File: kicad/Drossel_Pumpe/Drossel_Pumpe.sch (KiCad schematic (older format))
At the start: 6 parts, among them J1 Conn_02x01, M1 Pumpe

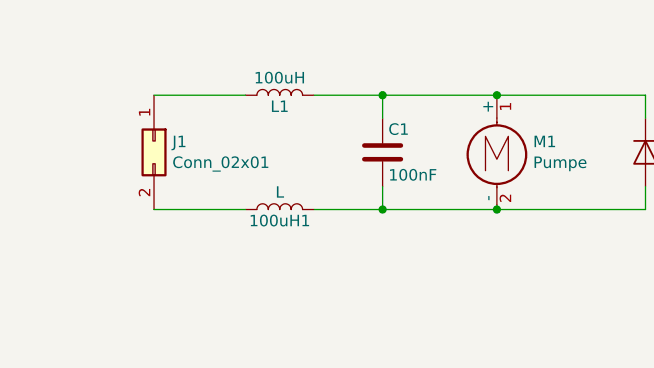
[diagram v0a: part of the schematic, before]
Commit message: umbenannt:      2019_Abschlussprojekt_Zuordnugstabelle.ods -> Doku/2019_Abschlussprojekt_Zuordnugstabelle.ods 	neue Datei:     Doku/Anmerungen_fuer_Doku.odt 	umbenannt:      Stueckliste.ods -> Doku/Stueckliste.ods 	geändert:       abschlussprojekt/abschlussprojekt.ino 	geändert:       kicad/Drossel_Pumpe/Drossel_Pumpe.bak 	geändert:       kicad/Drossel_Pumpe/Drossel_Pumpe.pdf 	geändert:       kicad/Drossel_Pumpe/Drossel_Pumpe.sch 	geändert:       kicad/dsub_1/dsub_1-cache.lib 	neue Datei:     kicad/dsub_1/dsub_1.bak 	geändert:       kicad/dsub_1/dsub_1.pdf 	geändert:       kicad/dsub_1/dsub_1.pro 	geändert:       kicad/dsub_1/dsub_1.sch
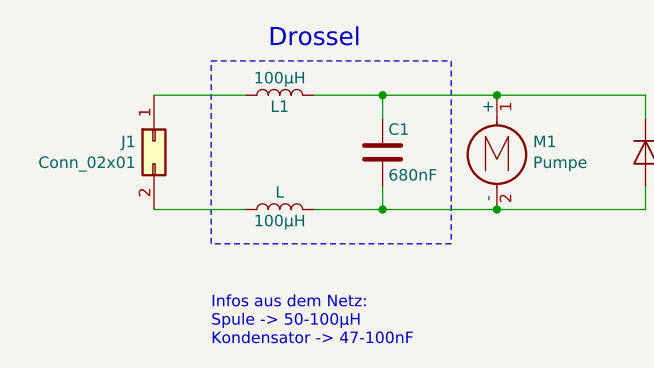
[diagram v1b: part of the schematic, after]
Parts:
- C1: value 100nF -> 680nF
- L1: value 100uH -> 100µH
- renumbered 100uH1 to 100µH
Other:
- note added: "Drossel"
- note added: "Infos aus dem Netz:\nSpule -> 50-100µH\nKondensator -> 47-100nF"
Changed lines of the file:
@@
 EESchema Schematic File Version 4
 LIBS:Drossel_Pumpe-cache
-EELAYER 29 0
+EELAYER 26 0
 EELAYER END
 $Descr A4 11693 8268
 encoding utf-8
 Sheet 1 1
-Title "HF-Entstörung Wasserpumpe"
+Title "Entstördrosseln für die Wasserpumpe"
 Date "2019-07-10"
-Rev ""
-Comp ""
-Comment1 ""
+Rev "0.2"
+Comp "STB AEA8"
+Comment1 "Nawroth, Graf, Roth"
 Comment2 ""
 Comment3 ""
@@
 P 6400 2700
 F 0 "L1" V 6350 2700 50  0000 C CNN
-F 1 "100uH" V 6475 2700 50  0000 C CNN
+F 1 "100µH" V 6475 2700 50  0000 C CNN
 F 2 "" H 6400 2700 50  0001 C CNN
 F 3 "" H 6400 2700 50  0001 C CNN
@@
 P 6850 2950
 F 0 "C1" H 6875 3050 50  0000 L CNN
-F 1 "100nF" H 6875 2850 50  0000 L CNN
+F 1 "680nF" H 6875 2850 50  0000 L CNN
 F 2 "" H 6888 2800 50  0001 C CNN
 F 3 "" H 6850 2950 50  0001 C CNN
@@
 $EndComp
 $Comp
-L Drossel_Pumpe-rescue:L 100uH1
+L Drossel_Pumpe-rescue:L 100µH
 U 1 1 5D25B187
 P 6400 3200
-F 0 "100uH1" V 6350 3200 50  0000 C CNN
+F 0 "100µH" V 6350 3200 50  0000 C CNN
 F 1 "L" V 6475 3200 50  0000 C CNN
 F 2 "" H 6400 3200 50  0001 C CNN
@@
 F 3 "~" H 5850 2900 50  0001 C CNN
 	1    5850 2900
-	0    1    1    0
+	0    -1   1    0
 $EndComp
 Wire Wire Line
@@
 	8000 3200 7350 3200
 Connection ~ 7350 3200
+Wire Notes Line
+	6100 2550 7150 2550
+Wire Notes Line
+	7150 2550 7150 3350
+Wire Notes Line
+	7150 3350 6100 3350
+Wire Notes Line
+	6100 3350 6100 2550
+Text Notes 6350 2500 0    79   ~ 0
+Drossel
+Text Notes 6100 3800 0    50   ~ 0
+Infos aus dem Netz:\nSpule -> 50-100µH\nKondensator -> 47-100nF
 $EndSCHEMATC

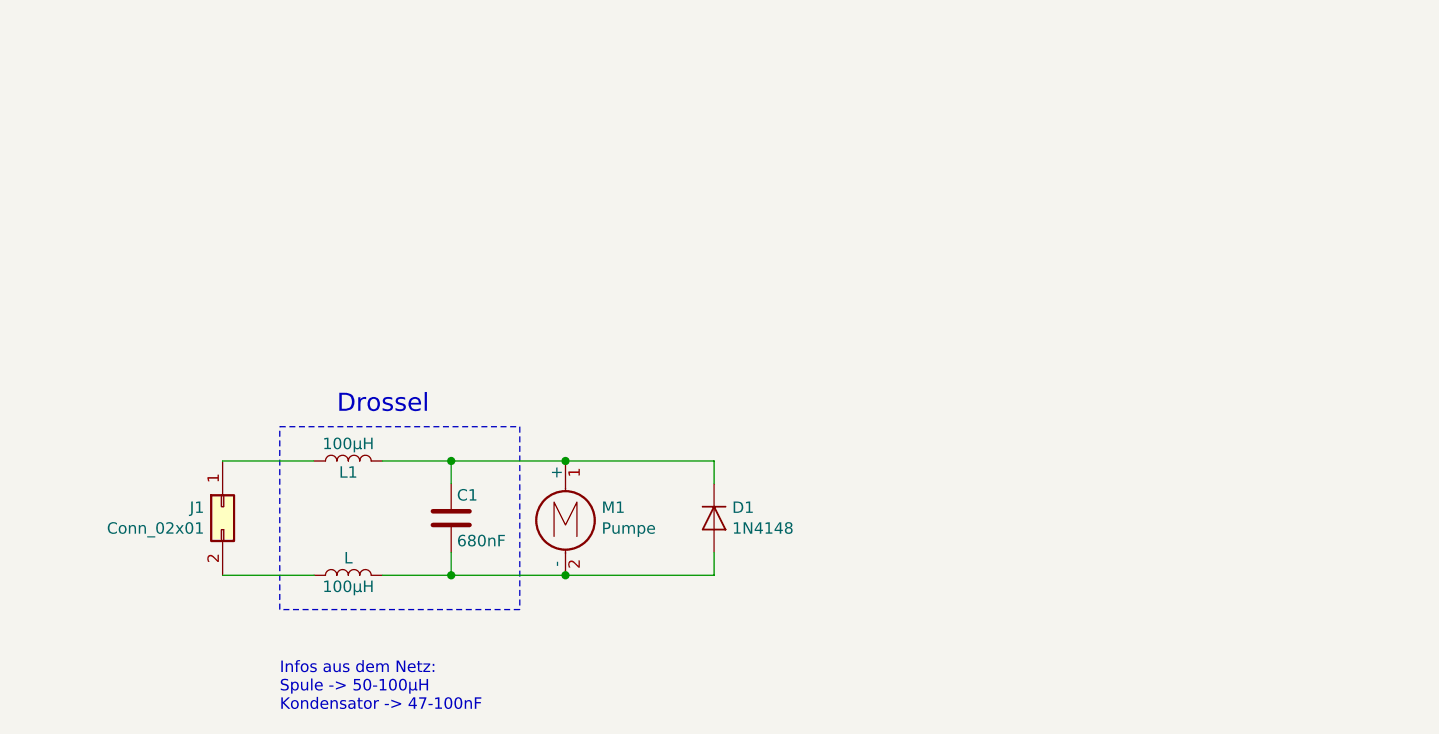
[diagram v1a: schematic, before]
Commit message: geändert:       abschlussprojekt/abschlussprojekt.ino -> Heizung, 	geändert:       kicad/Drossel_Pumpe/Drossel_Pumpe-cache.lib 	geändert:       kicad/Drossel_Pumpe/Drossel_Pumpe.bak 	geändert:       kicad/Drossel_Pumpe/Drossel_Pumpe.pdf 	geändert:       kicad/Drossel_Pumpe/Drossel_Pumpe.sch
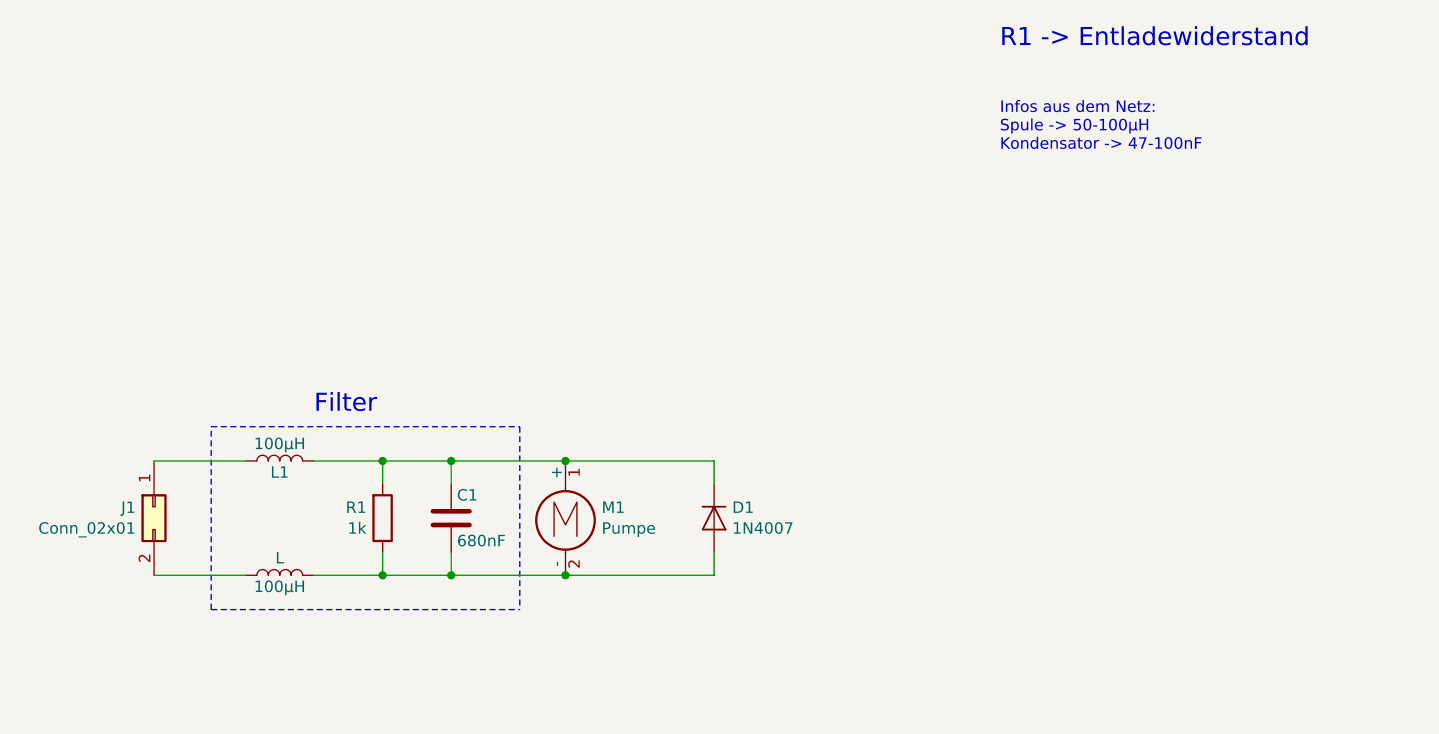
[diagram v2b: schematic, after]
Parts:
- added R1: 1k, symbol Device:R
- D1: value 1N4148 -> 1N4007
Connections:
- net at C1.1, D1.1 (K), L1.2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: now also R1.2
- net at 100µH.2, C1.2, D1.2 (A)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: now also R1.1
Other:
- note added: "Filter"
- note added: "R1 -> Entladewiderstand"
- note removed: "Drossel"
- moved on the sheet: 100µH, J1, L1
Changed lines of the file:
@@
 L Drossel_Pumpe-rescue:L L1
 U 1 1 5D25B130
-P 6400 2700
-F 0 "L1" V 6350 2700 50  0000 C CNN
-F 1 "100µH" V 6475 2700 50  0000 C CNN
-F 2 "" H 6400 2700 50  0001 C CNN
-F 3 "" H 6400 2700 50  0001 C CNN
-	1    6400 2700
+P 6100 2700
+F 0 "L1" V 6050 2700 50  0000 C CNN
+F 1 "100µH" V 6175 2700 50  0000 C CNN
+F 2 "" H 6100 2700 50  0001 C CNN
+F 3 "" H 6100 2700 50  0001 C CNN
+	1    6100 2700
 	0    -1   -1   0
 $EndComp
@@
 L Drossel_Pumpe-rescue:L 100µH
 U 1 1 5D25B187
-P 6400 3200
-F 0 "100µH" V 6350 3200 50  0000 C CNN
-F 1 "L" V 6475 3200 50  0000 C CNN
-F 2 "" H 6400 3200 50  0001 C CNN
-F 3 "" H 6400 3200 50  0001 C CNN
-	1    6400 3200
+P 6100 3200
+F 0 "100µH" V 6050 3200 50  0000 C CNN
+F 1 "L" V 6175 3200 50  0000 C CNN
+F 2 "" H 6100 3200 50  0001 C CNN
+F 3 "" H 6100 3200 50  0001 C CNN
+	1    6100 3200
 	0    -1   -1   0
 $EndComp
@@
 L Connector_Generic:Conn_02x01 J1
 U 1 1 5D25E2D9
-P 5850 2900
-F 0 "J1" V 5854 2980 50  0000 L CNN
-F 1 "Conn_02x01" V 5945 2980 50  0000 L CNN
-F 2 "" H 5850 2900 50  0001 C CNN
-F 3 "~" H 5850 2900 50  0001 C CNN
-	1    5850 2900
+P 5550 2900
+F 0 "J1" V 5554 2980 50  0000 L CNN
+F 1 "Conn_02x01" V 5645 2980 50  0000 L CNN
+F 2 "" H 5550 2900 50  0001 C CNN
+F 3 "~" H 5550 2900 50  0001 C CNN
+	1    5550 2900
 	0    -1   1    0
 $EndComp
 Wire Wire Line
-	5850 2700 6250 2700
+	5550 2700 5950 2700
 Wire Wire Line
-	6550 2700 6850 2700
+	6250 2700 6550 2700
 Wire Wire Line
-	6850 3200 6550 3200
-Wire Wire Line
-	5850 3200 6250 3200
+	5550 3200 5950 3200
 Wire Wire Line
 	6850 2800 6850 2700
@@
 Wire Wire Line
 	7350 2700 6850 2700
-Connection ~ 6850 2700
 Wire Wire Line
 	7350 3200 6850 3200
-Connection ~ 6850 3200
 $Comp
 L Device:D D1
@@
 P 8000 2950
 F 0 "D1" V 7954 3029 50  0000 L CNN
-F 1 "1N4148" V 8045 3029 50  0000 L CNN
+F 1 "1N4007" V 8045 3029 50  0000 L CNN
 F 2 "" H 8000 2950 50  0001 C CNN
 F 3 "~" H 8000 2950 50  0001 C CNN
@@
 Connection ~ 7350 3200
 Wire Notes Line
-	6100 2550 7150 2550
-Wire Notes Line
 	7150 2550 7150 3350
 Wire Notes Line
-	7150 3350 6100 3350
+	5800 3350 5800 2550
+Text Notes 6250 2500 0    79   ~ 0
+Filter
+Text Notes 9250 1350 0    50   ~ 0
+Infos aus dem Netz:\nSpule -> 50-100µH\nKondensator -> 47-100nF
+$Comp
+L Device:R R1
+U 1 1 5D7D1E88
+P 6550 2950
+F 0 "R1" H 6480 2904 50  0000 R CNN
+F 1 "1k" H 6480 2995 50  0000 R CNN
+F 2 "" V 6480 2950 50  0001 C CNN
+F 3 "~" H 6550 2950 50  0001 C CNN
+	1    6550 2950
+	1    0    0    1
+$EndComp
+Wire Wire Line
+	6550 2800 6550 2700
+Wire Wire Line
+	6550 2700 6850 2700
+Connection ~ 6550 2700
+Connection ~ 6850 2700
+Wire Wire Line
+	6250 3200 6550 3200
+Connection ~ 6850 3200
+Wire Wire Line
+	6550 3100 6550 3200
+Connection ~ 6550 3200
+Wire Wire Line
+	6550 3200 6850 3200
 Wire Notes Line
-	6100 3350 6100 2550
-Text Notes 6350 2500 0    79   ~ 0
-Drossel
-Text Notes 6100 3800 0    50   ~ 0
-Infos aus dem Netz:\nSpule -> 50-100µH\nKondensator -> 47-100nF
+	5800 2550 7150 2550
+Wire Notes Line
+	5800 3350 7150 3350
+Text Notes 9250 900  0    79   ~ 0
+R1 -> Entladewiderstand
 $EndSCHEMATC
